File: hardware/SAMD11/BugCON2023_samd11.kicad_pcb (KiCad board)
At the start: 2 copper layers, 122.4 x 97.9 mm, 58 parts, among them J1 I2C, J5 Serial, P1 USB_C_Plug_USB2.0, Q1 DMG3415U-7, SW1 RESET, SW2 ON, SW3 SW_Push, SW4 SW_Push, U1 W25Q16JV, U2 AP2112K-3.3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

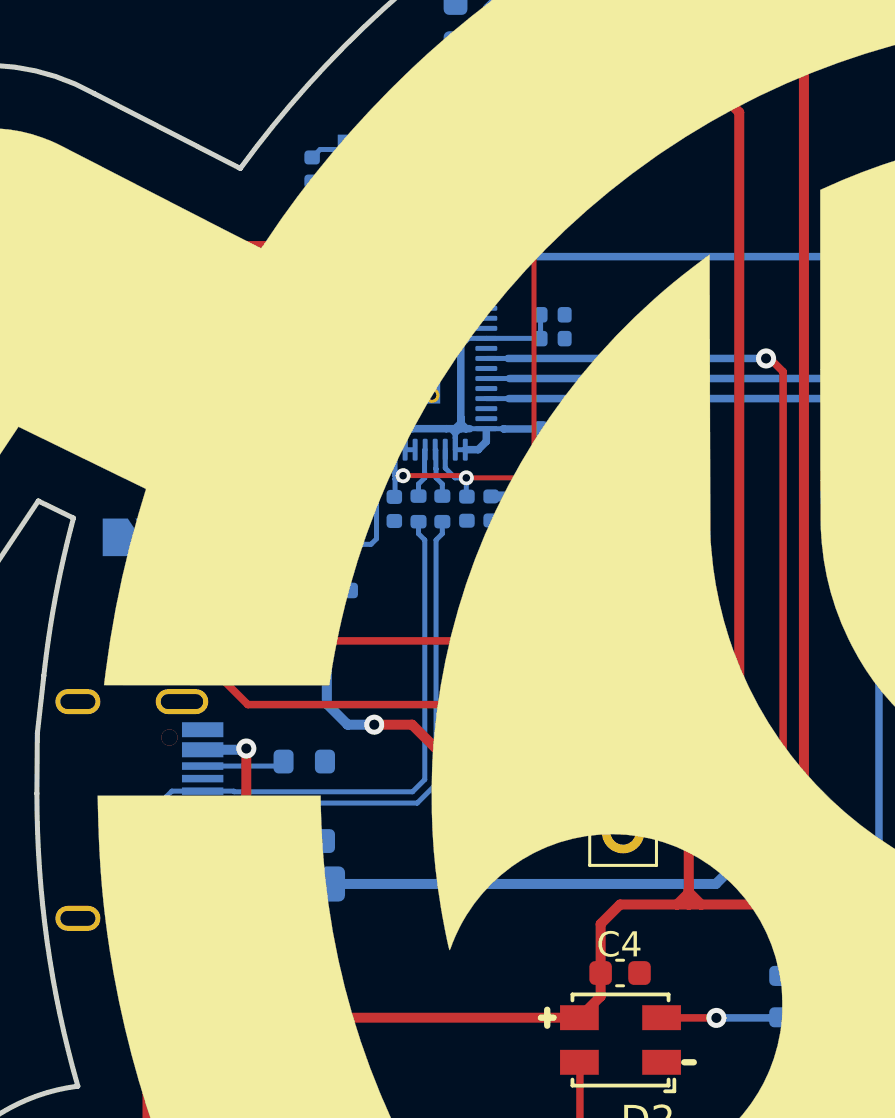
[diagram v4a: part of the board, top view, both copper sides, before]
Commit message: upd BOM and upd silkscreen on RP2040
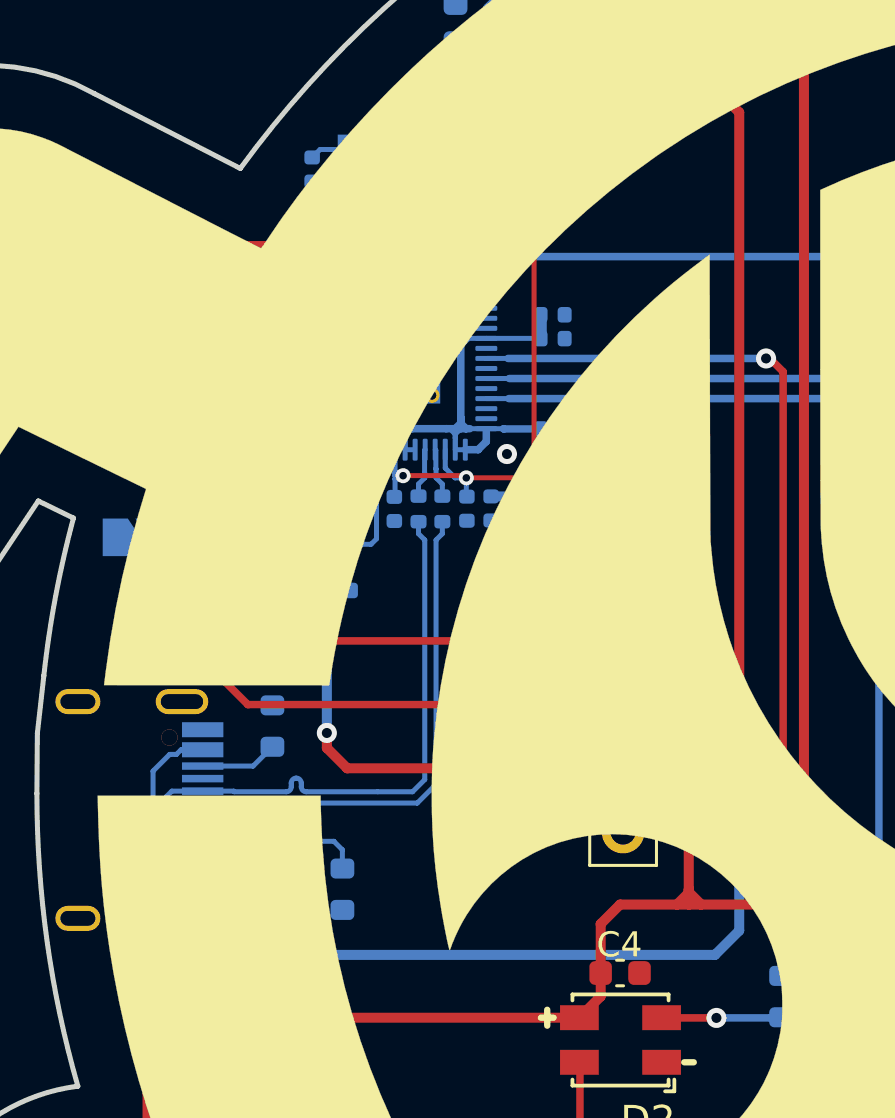
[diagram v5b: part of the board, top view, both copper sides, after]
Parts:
- R10: value 10k -> 10K; footprint Resistor_SMD:R_0402_1005Metric -> Resistor_SMD:R_0603_1608Metric
- moved R1 2.45 mm to (120.3, 105.9), turned to 90 degrees
- moved F1 2.17 mm to (118.0, 107.6), turned to -90 degrees
- moved R2 1.90 mm to (117.6, 99.4), turned to -90 degrees
- moved R10 0.40 mm to (116.8, 94.1)
- moved C11 0.10 mm to (124.7, 77.2)
- renumbered SW1 to RESET
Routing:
- net VBUS: track 67.2 -> 72.0 mm
- net Net-(P1-CC): track 3.23 -> 6.46 mm
- net Net-(F1-Pad1): track 10.2 -> 11.9 mm, vias 2 -> 0
- net /D+: track 23.1 -> 23.8 mm
- net /D-: track 24.1 -> 23.4 mm
- net GND: vias 1 -> 2

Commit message: add labels
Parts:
- added kibuzzard-6536B42E: G***, kibuzzard-6536B42E, B.Cu at (104.6, 87.1)
- added kibuzzard-6536B43C: G***, kibuzzard-6536B43C, B.Cu at (103.1, 89.7)
- added kibuzzard-6536B448: G***, kibuzzard-6536B448, B.Cu at (101.9, 91.9)
- added kibuzzard-6536B493: G***, kibuzzard-6536B493, B.Cu at (112.0, 89.2)
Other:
- board text removed: "GND"
- board text removed: "RX"
- board text removed: "TX"

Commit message: change buttons to the front and remove pull up resistors
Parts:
- removed R11, R12: 10K, Resistor_SMD:R_0603_1608Metric
- removed kibuzzard-6536B42E: G***, kibuzzard-6536B42E
- removed kibuzzard-6536B43C: G***, kibuzzard-6536B43C
- removed kibuzzard-6536B448: G***, kibuzzard-6536B448
- removed kibuzzard-6536B493: G***, kibuzzard-6536B493
- SW3, SW4: moved to F.Cu
- turned SW3 to -35 degrees
- turned SW4 to 35 degrees
- renumbered RESET to SW1
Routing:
- net +3.3V: track 338.9 -> 255.9 mm, vias 4 -> 2
- net /PB1: vias 0 -> 1
- net /PB2: vias 0 -> 1
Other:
- board text added: "GND"
- board text added: "RX"
- board text added: "TX"

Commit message: Add logos
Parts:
- added G***: LOGO, ElectronicCats:electronic_cats_logo_8x6, B.Cu at (118.4, 121.9)
- added REF**: OSHW-Logo2_9.8x8mm_SilkScreen, Symbol:OSHW-Logo2_9.8x8mm_SilkScreen, B.Cu at (134.1, 122.7)
- added REF**: KiCad-Logo2_5mm_SilkScreen, Symbol:KiCad-Logo2_5mm_SilkScreen, B.Cu at (132.6, 132.8)
- added kibuzzard-652EA30A: G***, kibuzzard-652EA30A, B.Cu at (137.9, 90.4)
- added kibuzzard-652EA51A: G***, kibuzzard-652EA51A, F.Cu at (119.1, 116.3)
- added kibuzzard-652EA51A: G***, kibuzzard-652EA51A, B.Cu at (126.5, 116.1)
- added kibuzzard-6536E385: G***, kibuzzard-6536E385, B.Cu at (126.5, 112.3)
- added kibuzzard-6536E415: G***, kibuzzard-6536E415, B.Cu at (105.7, 87.4)
- added kibuzzard-6536E422: G***, kibuzzard-6536E422, B.Cu at (103.9, 90.2)
- added kibuzzard-6536E42E: G***, kibuzzard-6536E42E, B.Cu at (102.9, 92.5)
- added kibuzzard-6536E471: G***, kibuzzard-6536E471, B.Cu at (202.2, 88.1)
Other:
- board text removed: "GND"
- board text removed: "RX"
- board text removed: "TX"
